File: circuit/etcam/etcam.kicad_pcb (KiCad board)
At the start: 2 copper layers, 71 parts, among them J1 SWD_connector, J2 USB_connector, J3 ESC_signal_connector, J4 ESC_GND_connector, J5 MCU_PWR_SRC_selector, J6 jumper_park, SW1 reset_SW, U1 FT232RL, U2 Si8640BB-B-IS1, U3 Si8640BB-B-IS1, U4 Si8640BB-B-IS1, U5 Si8640BB-B-IS1, U6 74HC251, U7 STM32F303xD/E-LQFP64, U8 LM1117-3.3, U9 ADuM5020, Y1 8MHz

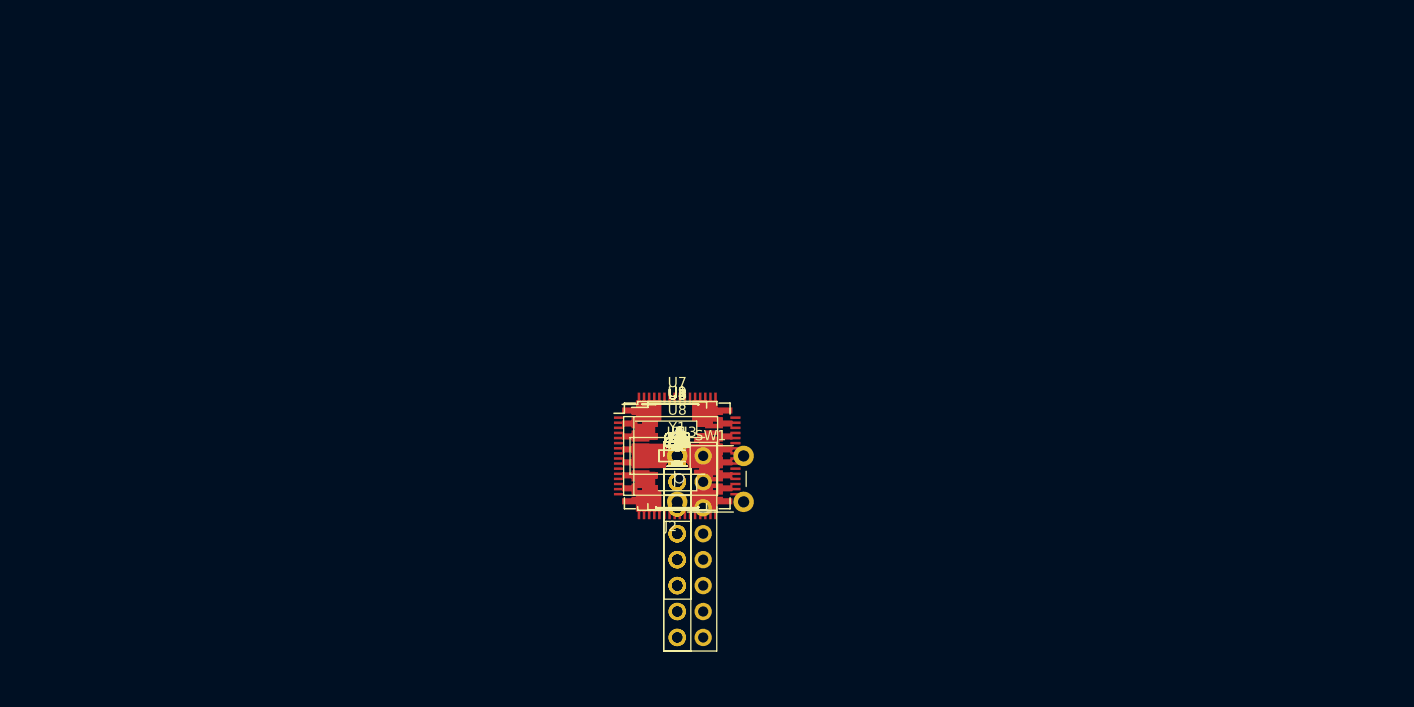
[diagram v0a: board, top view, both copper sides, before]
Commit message: added LEDs to every power rail of ETCAM and re-annotated the schematic
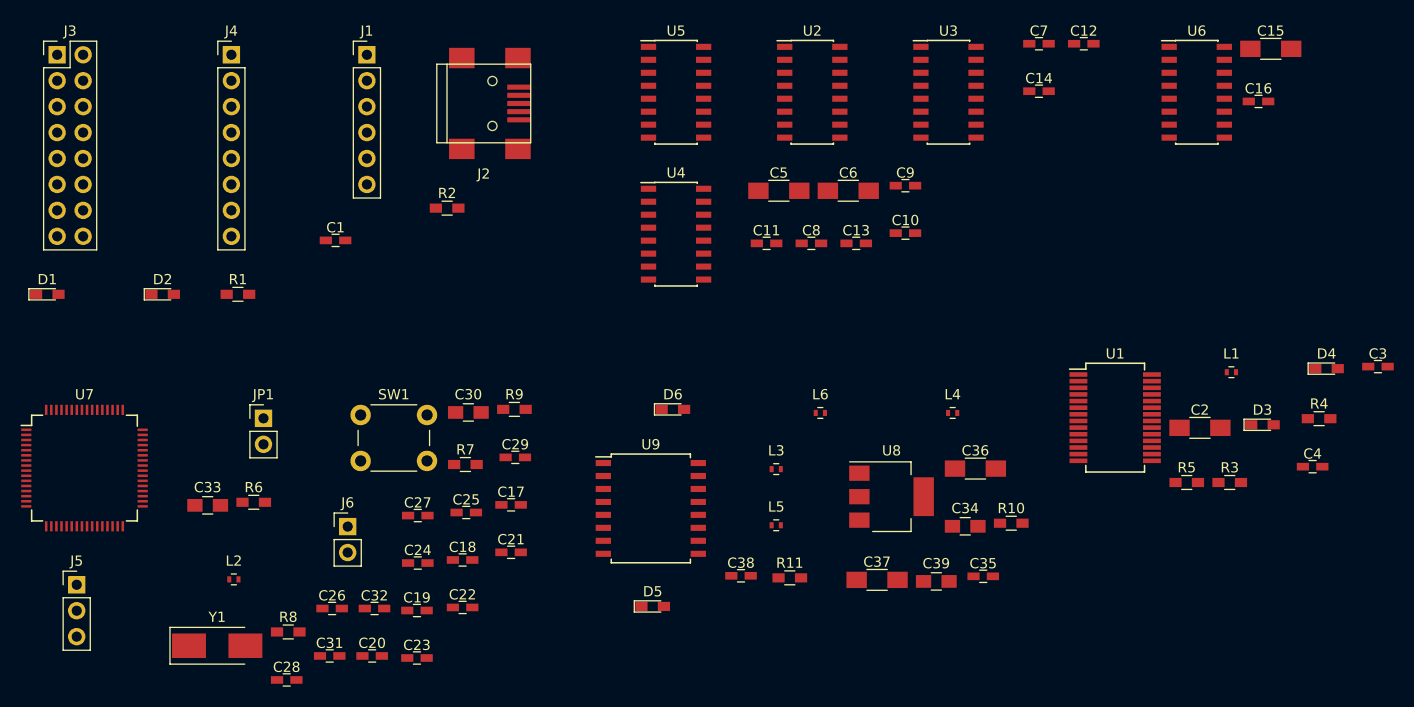
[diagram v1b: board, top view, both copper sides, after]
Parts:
- added C39: 10uF, Capacitors_SMD:C_0805_HandSoldering, F.Cu at (173.9, 117.3)
- added D3: TX_LED, LEDs:LED_0603_HandSoldering, F.Cu at (205.8, 102.0)
- added D4: RX_LED, LEDs:LED_0603_HandSoldering, F.Cu at (212.1, 96.5)
- added D5: +3.3V_USB_LED, LEDs:LED_0603_HandSoldering, F.Cu at (146.1, 119.7)
- added D6: +3.3V_ISOLATOR_LED, LEDs:LED_0603_HandSoldering, F.Cu at (148.1, 100.4)
- added R10: 330, Resistors_SMD:R_0603_HandSoldering, F.Cu at (181.2, 111.6)
- added R11: 330, Resistors_SMD:R_0603_HandSoldering, F.Cu at (159.5, 116.9)
- added R8: 10k, Resistors_SMD:R_0603_HandSoldering, F.Cu at (110.4, 122.2)
- added R9: 10k, Resistors_SMD:R_0603_HandSoldering, F.Cu at (132.6, 100.4)
- C15, C5: value 0.1uF -> 1uF; footprint Capacitors_SMD:C_0603_HandSoldering -> Capacitors_SMD:C_1206_HandSoldering
- C2: value 1uF -> 4.7uF
- C27: value 22pF -> 0.1uF
- C28: value 0.1uF -> 22pF
- C29: value 4.7uF -> 0.1uF; footprint Capacitors_SMD:C_0805_HandSoldering -> Capacitors_SMD:C_0603_HandSoldering
- C30: value 22pF -> 4.7uF; footprint Capacitors_SMD:C_0603_HandSoldering -> Capacitors_SMD:C_0805_HandSoldering
- C31: value 10nF -> 22pF
- C32: value 1uF -> 10nF; footprint Capacitors_SMD:C_0805_HandSoldering -> Capacitors_SMD:C_0603_HandSoldering
- C33: value 10uF -> 1uF
- C34: value 0.1uF -> 10uF; footprint Capacitors_SMD:C_0603_HandSoldering -> Capacitors_SMD:C_0805_HandSoldering
- C35: value 10uF -> 0.1uF; footprint Capacitors_SMD:C_1206_HandSoldering -> Capacitors_SMD:C_0603_HandSoldering
- C37: value 0.22uF -> 10uF; footprint Capacitors_SMD:C_0603_HandSoldering -> Capacitors_SMD:C_1206_HandSoldering
- C38: value 10uF -> 0.22uF; footprint Capacitors_SMD:C_0805_HandSoldering -> Capacitors_SMD:C_0603_HandSoldering
- C4: value 4.7uF -> 0.1uF; footprint Capacitors_SMD:C_1206_HandSoldering -> Capacitors_SMD:C_0603_HandSoldering
- D1: value TX_LED -> +3.3V_SWD_LED
- D2: value RX_LED -> +5V_USB_LED
- R1: value 10k -> 1k
- R3: value 330 -> 10k
- R4, R5: value 10k -> 330
- moved J3 72.3 mm to (87.8, 65.7)
- moved C15 70.5 mm to (206.6, 65.1)
- moved C3 69.2 mm to (217.1, 96.3)
- moved C16 66.7 mm to (205.4, 70.3)
- moved D1 63.7 mm to (86.8, 89.2)
- moved R4 63.0 mm to (211.4, 101.4)
- moved C4 62.2 mm to (210.7, 106.1)
- moved U6 62.1 mm to (199.4, 69.4)
- moved J5 60.2 mm to (89.7, 117.6)
- moved J4 58.7 mm to (104.8, 65.7)
- moved U7 58.1 mm to (90.4, 106.2)
- moved C12 56.7 mm to (188.3, 64.6)
- moved L1 54.9 mm to (202.8, 96.8)
- moved R3 54.2 mm to (202.6, 107.6)
- moved C7 53.7 mm to (183.9, 64.6)
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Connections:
- C16 pad 1: /controller/+3.3V_CONTROLLER -> /+3.3V_USB
- C2 pad 1: /+3.3V_USB -> /usb_to_serial/+5V_FTDI
- C25 pad 1: /~RST -> /controller/+3.3V_CONTROLLER
- C26 pad 1: /controller/+3.3V_CONTROLLER -> /~RST
- C27 pad 1: Net-(C27-Pad1) -> /controller/+3.3V_CONTROLLER
- C28 pad 1: /controller/+3.3V_CONTROLLER -> Net-(C28-Pad1)
- C30 pad 1: Net-(C30-Pad1) -> /controller/+3.3V_CONTROLLER
- C31 pad 1: /controller/+3.3V_ANALOG -> Net-(C31-Pad1)
- C33 pad 1: /+5V_USB -> /controller/+3.3V_ANALOG
- C34 pad 1: Net-(C34-Pad1) -> /+5V_USB
- C34 pad 2: Net-(C34-Pad2) -> GND
- C35 pad 1: /+5V_USB -> Net-(C35-Pad1)
- C35 pad 2: GND -> Net-(C35-Pad2)
- C36 pad 1: /+3.3V_USB -> /+5V_USB
- C37 pad 1: Net-(C37-Pad1) -> /+3.3V_USB
- C37 pad 2: Net-(C37-Pad2) -> GND
- C38 pad 1: /+3.3V_ISOLATOR -> Net-(C38-Pad1)
- C38 pad 2: GNDPWR -> Net-(C38-Pad2)
- C4 pad 1: /usb_to_serial/+5V_FTDI -> /usb_to_serial/+3.3V_FTDI
- C5 pad 1: /usb_to_serial/+3.3V_FTDI -> /+3.3V_USB
- D1 pad 1: Net-(D1-Pad1) -> GND
- D2 pad 1: Net-(D2-Pad1) -> GND
- L3 pad 2: Net-(C34-Pad1) -> Net-(C35-Pad1)
- L4 pad 2: Net-(C34-Pad2) -> Net-(C35-Pad2)
- L5 pad 1: Net-(C37-Pad1) -> Net-(C38-Pad1)
- L6 pad 1: Net-(C37-Pad2) -> Net-(C38-Pad2)
- R1 pad 1: Net-(R1-Pad1) -> /+5V_USB
- R1 pad 2: /usb_to_serial/+5V_FTDI -> Net-(D2-Pad2)
- R2 pad 1: Net-(D1-Pad2) -> /+3.3V_SWD
- R2 pad 2: /usb_to_serial/+3.3V_FTDI -> Net-(D1-Pad2)
- R3 pad 1: Net-(D2-Pad2) -> Net-(R3-Pad1)
- R3 pad 2: /usb_to_serial/+3.3V_FTDI -> /usb_to_serial/+5V_FTDI
- R4 pad 1: /controller/BOOT0 -> Net-(D3-Pad2)
- R4 pad 2: GND -> /usb_to_serial/+3.3V_FTDI
- R5 pad 1: GND -> Net-(D4-Pad2)
- R5 pad 2: Net-(R5-Pad2) -> /usb_to_serial/+3.3V_FTDI
- R6 pad 1: GND -> /controller/BOOT0
- R6 pad 2: Net-(R5-Pad2) -> GND
- R7 pad 1: Net-(R7-Pad1) -> GND
- R7 pad 2: /controller/BOOT0 -> Net-(R7-Pad2)
- U1 pad 19: Net-(R1-Pad1) -> Net-(R3-Pad1)
- U1 pad 22: Net-(D2-Pad1) -> Net-(D4-Pad1)
- U1 pad 23: Net-(D1-Pad1) -> Net-(D3-Pad1)
- U7 pad 44: Net-(R5-Pad2) -> Net-(R7-Pad2)
- U7 pad 5: Net-(C27-Pad1) -> Net-(C28-Pad1)
- U7 pad 6: Net-(C30-Pad1) -> Net-(C31-Pad1)
- U7 pad 60: Net-(R7-Pad1) -> Net-(R9-Pad1)
- U9 pad 11: Net-(C37-Pad2) -> Net-(C38-Pad2)
- U9 pad 12: Net-(C37-Pad1) -> Net-(C38-Pad1)
- U9 pad 13: Net-(C37-Pad2) -> Net-(C38-Pad2)
- U9 pad 14: Net-(C37-Pad2) -> Net-(C38-Pad2)
- U9 pad 15: Net-(C37-Pad2) -> Net-(C38-Pad2)
- U9 pad 2: Net-(C34-Pad2) -> Net-(C35-Pad2)
- U9 pad 3: Net-(C34-Pad2) -> Net-(C35-Pad2)
- U9 pad 4: Net-(C34-Pad2) -> Net-(C35-Pad2)
- U9 pad 5: Net-(C34-Pad1) -> Net-(C35-Pad1)
- U9 pad 6: Net-(C34-Pad2) -> Net-(C35-Pad2)
- U9 pad 8: Net-(C34-Pad2) -> Net-(C35-Pad2)
- U9 pad 9: Net-(C37-Pad2) -> Net-(C38-Pad2)
- Y1 pad 1: Net-(C27-Pad1) -> Net-(C28-Pad1)
- Y1 pad 2: Net-(C30-Pad1) -> Net-(C31-Pad1)
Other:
- net class Default: clearance 0.0254 -> 0.127; trace_width 0.0254 -> 0.254
- rule trace_clearance: 0.0254 -> 0.127
- rule trace_min: 0.0254 -> 0.254

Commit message: finished routing ETCAM PCB without GND
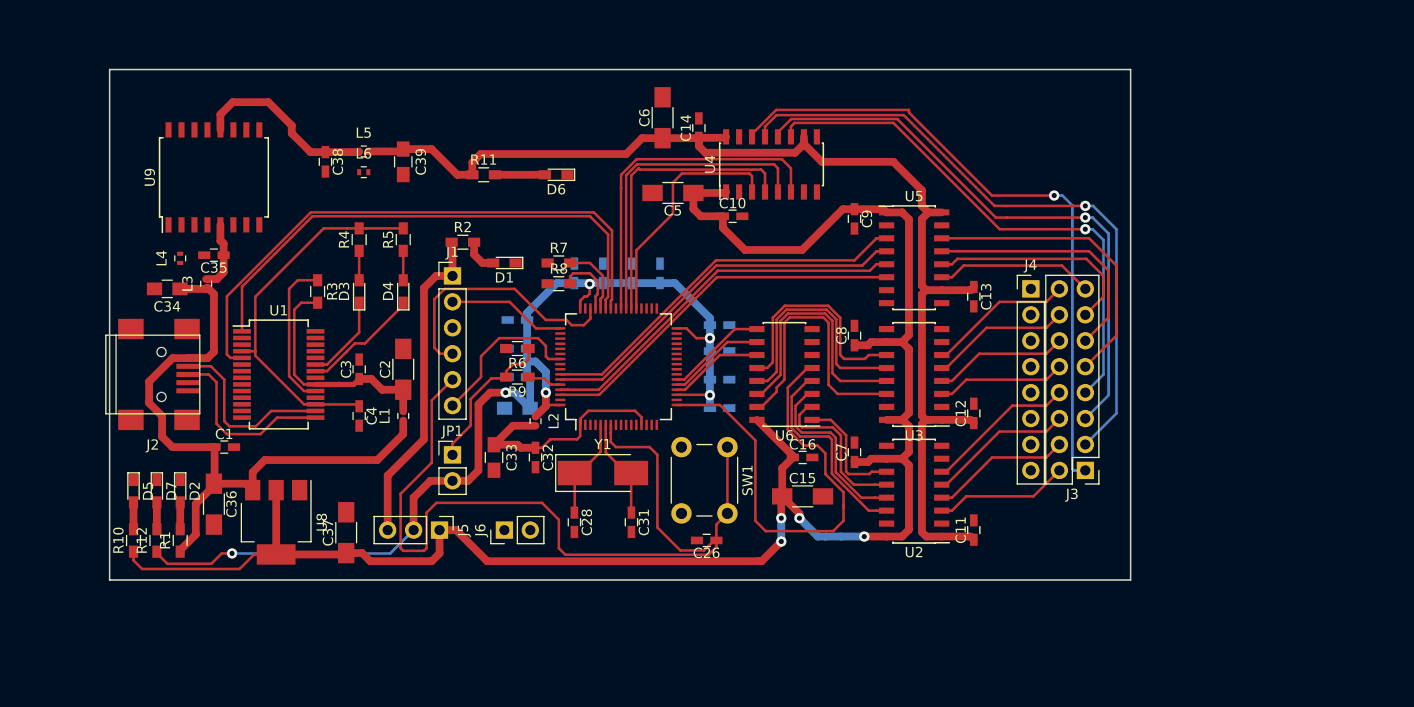
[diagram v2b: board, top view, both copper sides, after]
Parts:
- added D7: +3.3V_CONTROLLER_LED, LEDs:LED_0603_HandSoldering, F.Cu at (97.5, 108.5)
- added R12: 330, Resistors_SMD:R_0603_HandSoldering, F.Cu at (97.5, 113.3)
- C17, C18, C19, C20, C21, C22, C23, C24, C25, C27, C29, C30: moved to B.Cu
- moved J3 108.6 mm to (188.5, 106.4), turned to 180 degrees
- moved C3 99.8 mm to (117.3, 96.5), turned to 90 degrees
- moved R4 95.6 mm to (117.3, 83.8), turned to 90 degrees
- moved C4 93.5 mm to (117.3, 101.1), turned to 270 degrees
- moved R3 91.3 mm to (113.3, 88.9), turned to 270 degrees
- moved D4 90.7 mm to (121.7, 88.9), turned to 90 degrees
- moved D3 89.4 mm to (117.3, 88.9), turned to 90 degrees
- moved R10 86.0 mm to (95.2, 113.3), turned to 90 degrees
- moved U1 82.0 mm to (109.5, 97.0)
- moved C35 81.6 mm to (103.1, 85.3), turned to 180 degrees
- moved J4 81.6 mm to (183.1, 88.6)
- moved C34 81.5 mm to (98.6, 88.6), turned to 180 degrees
- moved L1 81.2 mm to (121.7, 101.1), turned to 90 degrees
- moved R5 80.3 mm to (121.7, 83.8), turned to 90 degrees
- moved C2 78.2 mm to (121.7, 96.5), turned to 90 degrees
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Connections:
- R8 pad 2: Net-(R7-Pad2) -> Net-(R8-Pad2)
- U7 pad 45: (no net) -> Net-(R8-Pad2)
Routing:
- net /+3.3V_USB: track 0.00 -> 179.1 mm, vias 0 -> 4
- net /+3.3V_ISOLATOR: track 0.00 -> 115.4 mm
- net /controller/+3.3V_CONTROLLER: track 0.00 -> 107.7 mm, vias 0 -> 6
- net /~RST: track 0.00 -> 88.9 mm
- net /+5V_USB: track 0.00 -> 64.3 mm
- net /ISOLATED_DSHOT1: track 0.00 -> 63.8 mm, vias 0 -> 1
- net /ISOLATED_DSHOT2: track 0.00 -> 63.3 mm, vias 0 -> 1
- net /ISOLATED_DSHOT3: track 0.00 -> 57.1 mm, vias 0 -> 1
- net /FTDI<--MCU: track 0.00 -> 56.8 mm
- net /ISOLATED_DSHOT4: track 0.00 -> 52.2 mm, vias 0 -> 1
- net /FTDI-->MCU: track 0.00 -> 51.2 mm
- net /telementry_selector/SELECTED_TELEMENTRY: track 0.00 -> 46.0 mm
- net /controller/DSHOT5: track 0.00 -> 37.5 mm
- net /controller/DSHOT6: track 0.00 -> 37.2 mm
- net /controller/DSHOT7: track 0.00 -> 37.0 mm
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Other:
- board outline added: 100 x 50 mm

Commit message: added mounting holes into ETCAM PCB
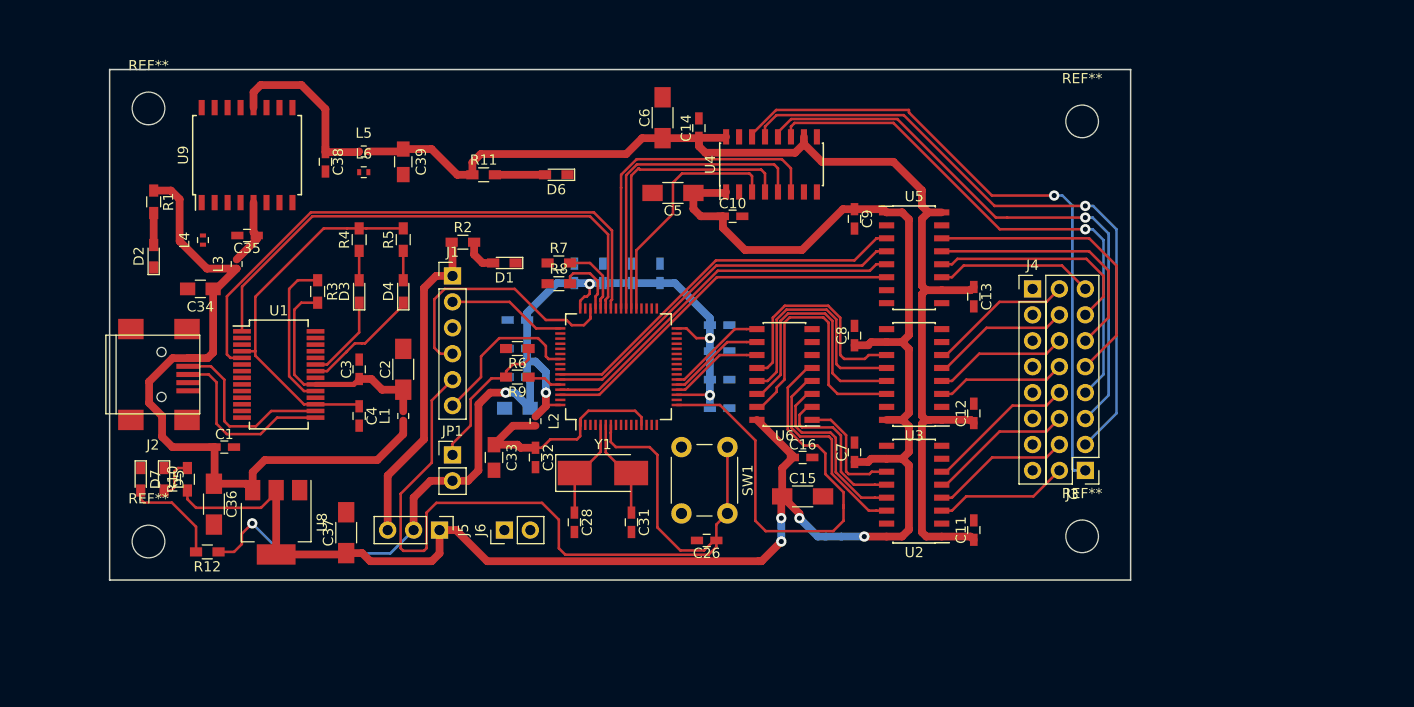
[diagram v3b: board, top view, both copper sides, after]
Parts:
- added REF**: MountingHole_3.2mm_M3, Mounting_Holes:MountingHole_3.2mm_M3, F.Cu at (188.2, 72.2)
- added REF**: MountingHole_3.2mm_M3, Mounting_Holes:MountingHole_3.2mm_M3, F.Cu at (188.2, 112.9)
- added REF**: MountingHole_3.2mm_M3, Mounting_Holes:MountingHole_3.2mm_M3, F.Cu at (96.7, 71.0)
- added REF**: MountingHole_3.2mm_M3, Mounting_Holes:MountingHole_3.2mm_M3, F.Cu at (96.7, 113.4)
- moved R1 33.3 mm to (97.2, 80.1), turned to 270 degrees
- moved D2 23.2 mm to (97.2, 85.4), turned to 90 degrees
- moved R10 7.98 mm to (100.5, 107.3)
- moved R12 5.06 mm to (102.5, 114.4), turned to 180 degrees
- moved U9 3.91 mm to (106.4, 75.5)
- moved C35 3.77 mm to (106.4, 83.4)
- moved L3 3.56 mm to (105.4, 86.2)
- moved C34 3.24 mm to (101.8, 88.6)
- moved D5 3.21 mm to (98.2, 107.3)
- moved L4 2.86 mm to (102.0, 83.9)
- moved D7 1.97 mm to (96.0, 107.3)
- moved J4 0.17 mm to (183.3, 88.6)
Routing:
- net Net-(D7-Pad2): track 2.63 -> 9.85 mm
- net /+5V_USB: track 64.3 -> 70.5 mm
- net /+3.3V_USB: track 179.1 -> 174.1 mm
- net /controller/+3.3V_CONTROLLER: track 107.7 -> 103.6 mm
- net Net-(D5-Pad2): track 2.63 -> 4.11 mm
- net Net-(C38-Pad1): track 18.1 -> 17.4 mm
- net Net-(D2-Pad2): track 2.63 -> 3.13 mm

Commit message: added descriptive silkskins to ETCAM PCB
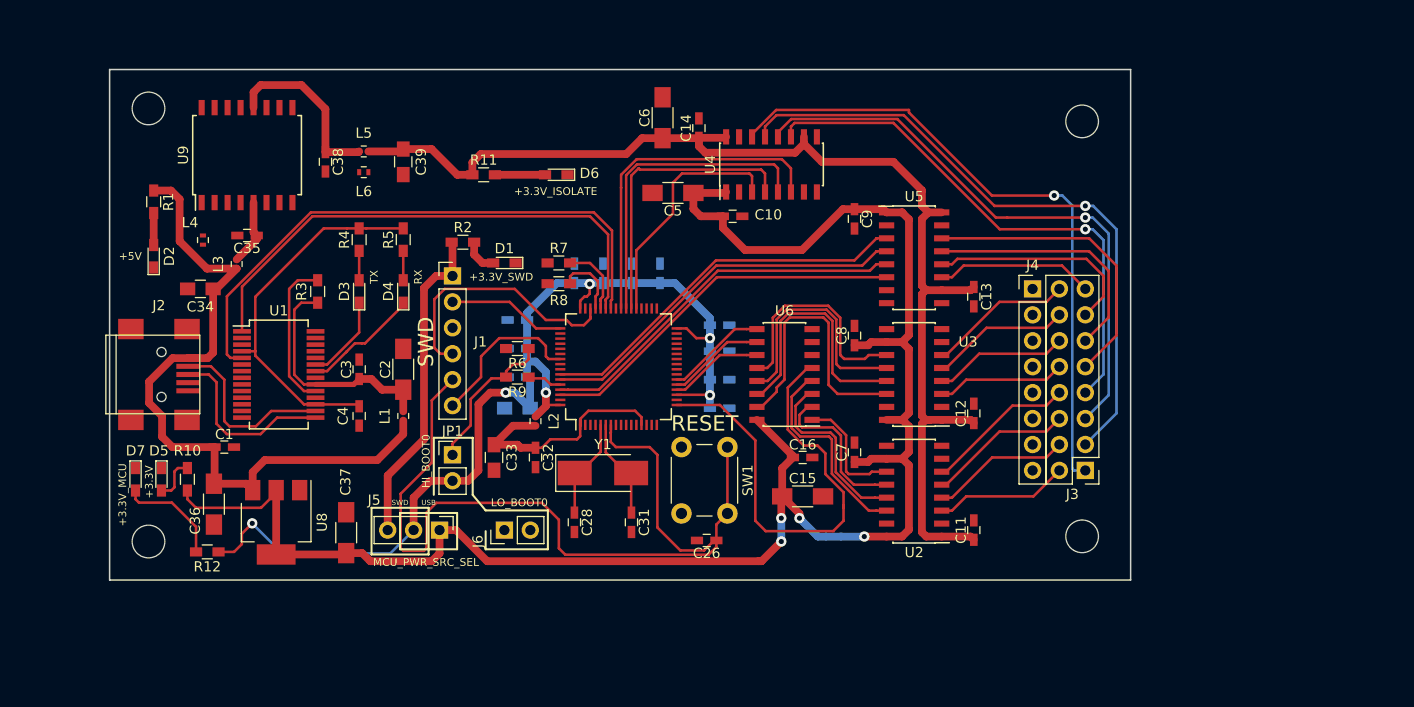
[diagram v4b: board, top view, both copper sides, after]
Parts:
- moved D7 0.51 mm to (95.4, 107.3)
- moved D5 0.25 mm to (98.0, 107.3)
- renumbered REF** to ?
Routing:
- net Net-(D7-Pad2): track 9.85 -> 10.4 mm
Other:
- board text added: "+3.3V"
- board text added: "+3.3V_ISOLATE"
- board text added: "+3.3V_MCU"
- board text added: "+3.3V_SWD"
- board text added: "+5V"
- board text added: "HI_BOOT0"
- board text added: "LO_BOOT0"
- board text added: "MCU_PWR_SRC_SEL"
- board text added: "RESET"
- board text added: "RX"
- board text added: "SWD"
- board text added: "TX"
- board text added: "USB"

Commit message: added GND plane to ETCAM PCB
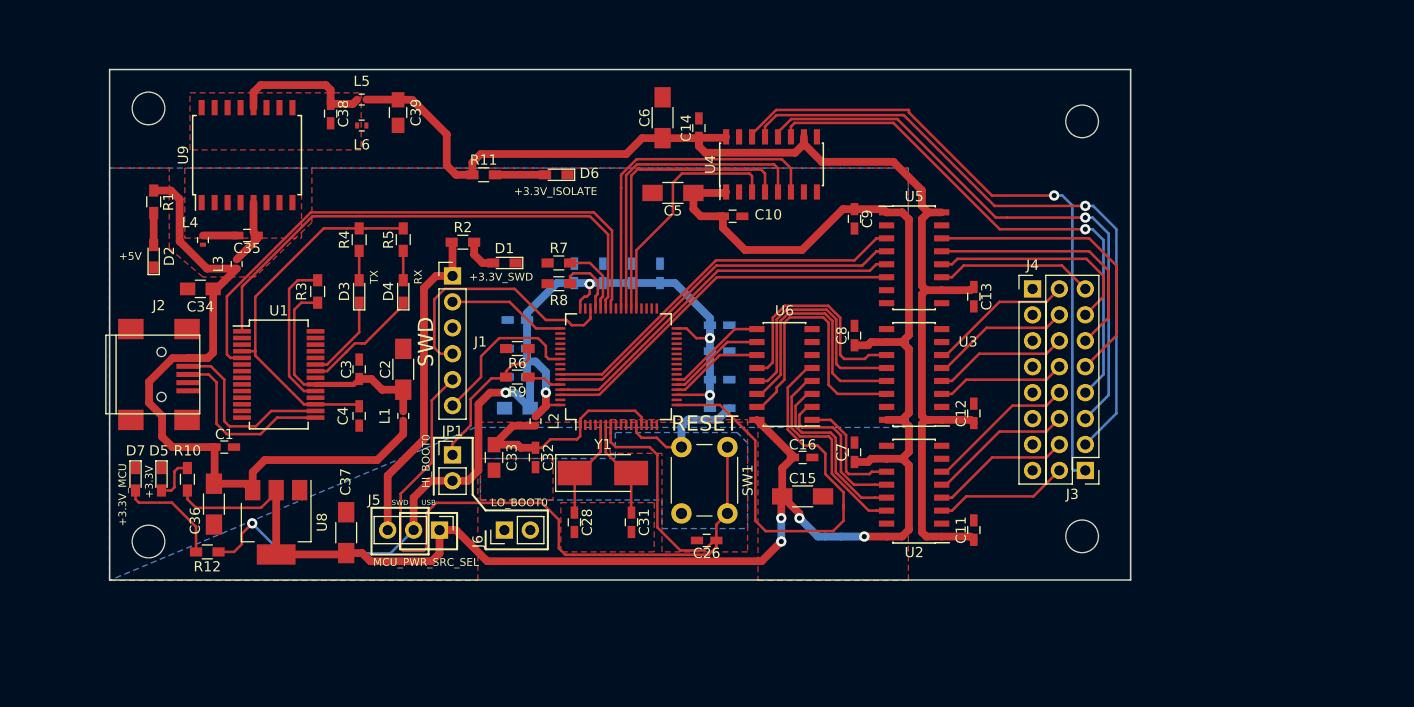
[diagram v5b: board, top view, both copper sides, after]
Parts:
- moved L5 5.08 mm to (117.6, 70.1)
- moved C39 4.85 mm to (121.2, 71.4)
- moved C38 4.75 mm to (114.6, 71.5)
- moved L6 4.58 mm to (117.6, 72.6)
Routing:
- net GND: track 0.00 -> 13.2 mm
- net /+3.3V_ISOLATOR: track 115.4 -> 119.2 mm
- net Net-(C38-Pad1): track 17.4 -> 13.7 mm
- net Net-(C35-Pad2): track 0.00 -> 3.37 mm
- added copper zone on B.Cu, net GND
- added copper zone on F.Cu, net GND
- added copper zone on F.Cu, net Net-(C35-Pad2)
- added copper zone on F.Cu, net Net-(C38-Pad2)
